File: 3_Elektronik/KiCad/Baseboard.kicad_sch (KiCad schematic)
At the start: 72 parts, among them J1 Conn_02x10_Odd_Even, J2 Conn_02x10_Odd_Even, J3 Conn_02x10_Odd_Even, J4 Conn_02x10_Odd_Even, J5 PinHeader 2,54mm 3p, J6 693072010801, J7 629722000214, Q1 2N7002K, Q2 2N7002K, SW2 430481025816, U1 ADXL375BCCZ, U2 TPS7B8601QDDARQ1, U3 TCAN334, U4 ESP32-S3-WROOM-1, U5 LSM6DSO32XTR, U6 DPS310, U7 MLX90395xLW, U8 CH224A

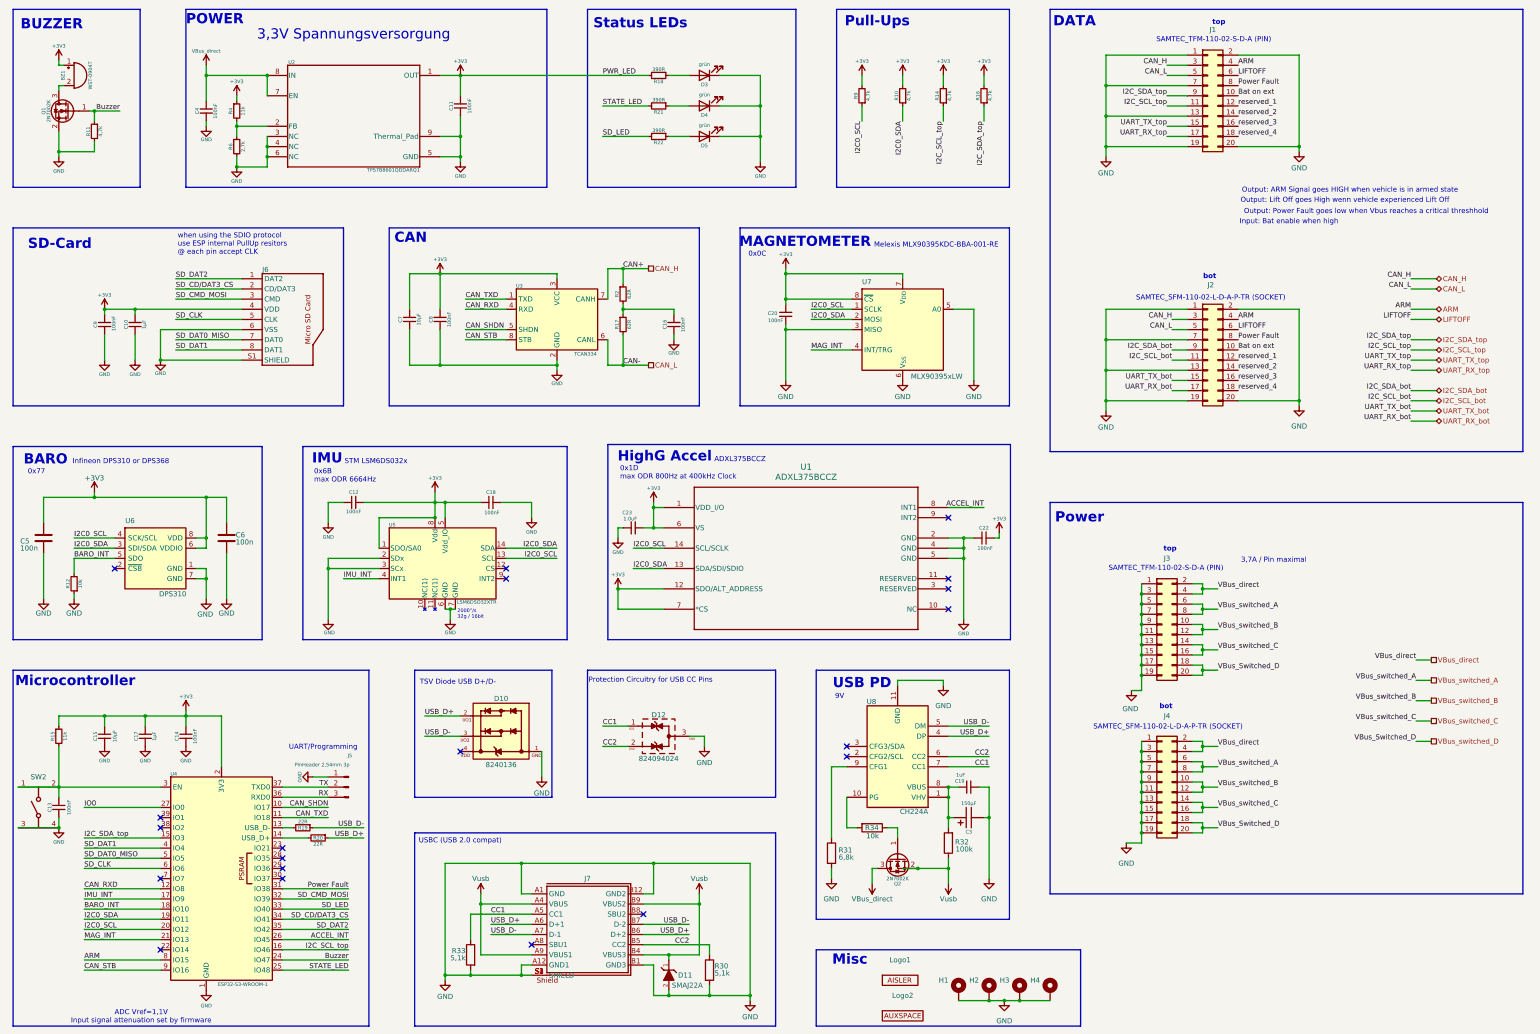
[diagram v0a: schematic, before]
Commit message: electronics: :sparkles: add BOOTSEL
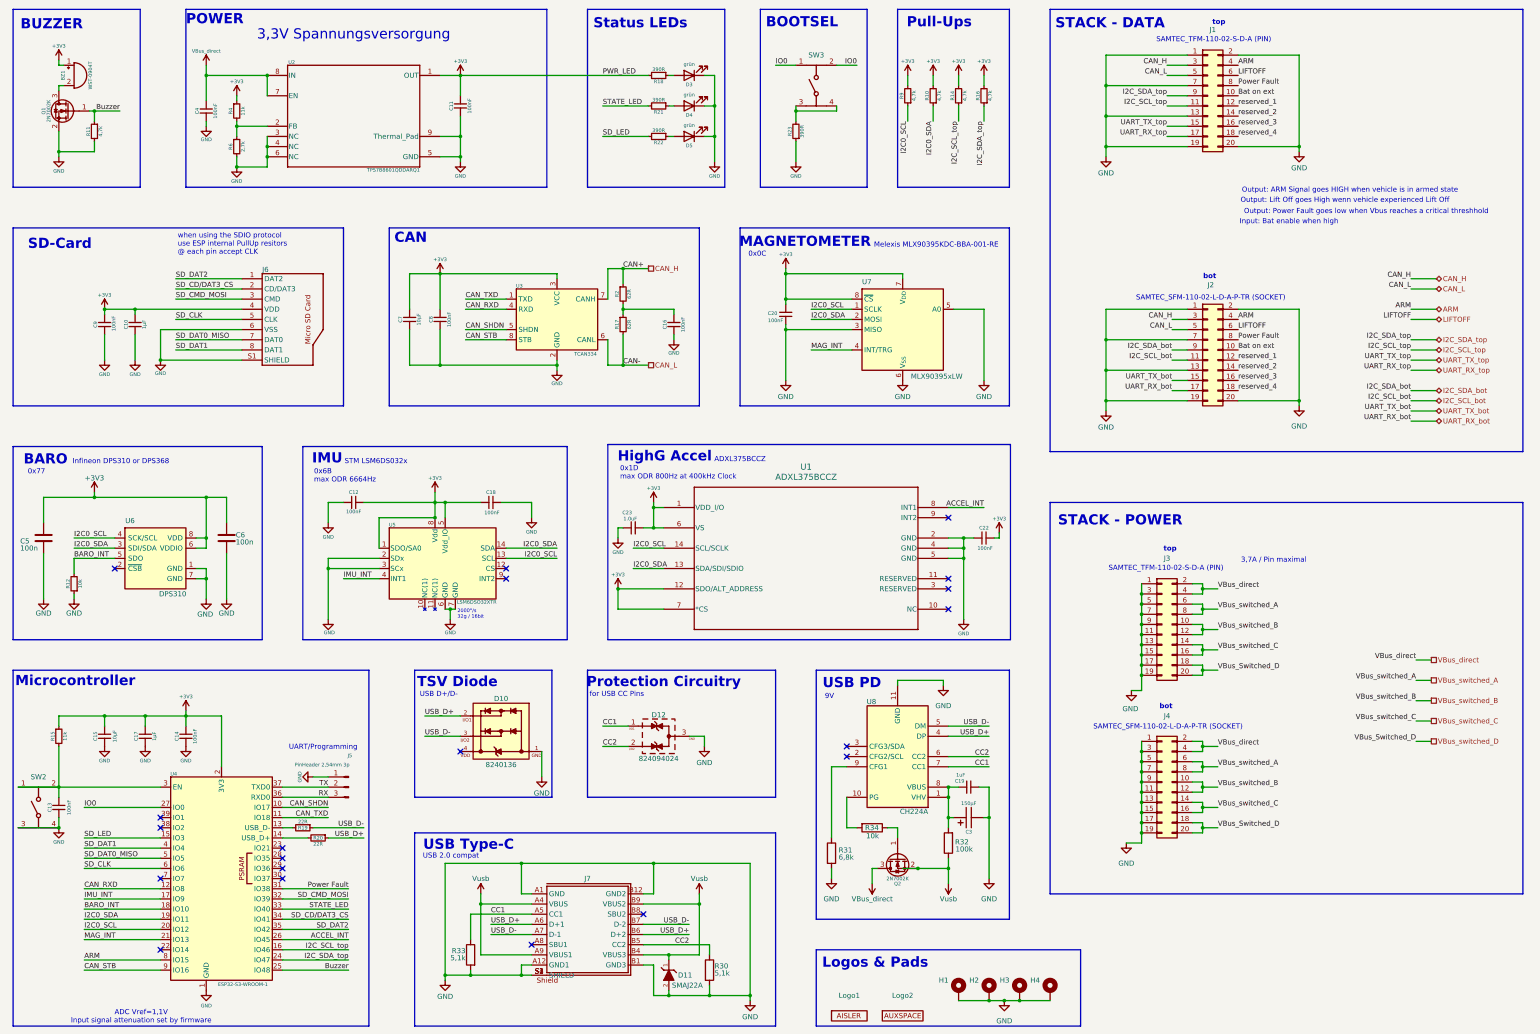
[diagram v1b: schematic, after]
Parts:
- added R23: 390R, Resistor_SMD:R_0603_1608Metric, symbol Device:R_Small
- added SW3: 430481025816, AUXSPACE:SW_Wurth_WS-TASV_430481025816, symbol AUXSPACE:430481025816
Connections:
- net Buzzer: now also U4.25 (IO48); no longer U4.24 (IO47)
- net GND: now also R23.1
- net I2C_SDA_top: now also U4.24 (IO47); no longer U4.15 (IO3)
- net IO0: now also SW3.1, SW3.2
- net SD_LED: now also U4.15 (IO3); no longer U4.33 (IO40)
- net STATE_LED: now also U4.33 (IO40); no longer U4.25 (IO48)
- new net: R23.2, SW3.3, SW3.4
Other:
- note added: "BOOTSEL"
- note added: "Logos & Pads"
- note added: "Protection Circuitry"
- note added: "STACK - DATA"
- note added: "STACK - POWER"
- note added: "TSV Diode"
- note added: "USB 2.0 compat"
- note added: "USB D+/D-"
- note added: "USB Type-C"
- note added: "for USB CC Pins"
- note removed: "DATA"
- note removed: "Misc"
- note removed: "Power"
- note removed: "Protection Circuitry for USB CC Pins"
- note removed: "TSV Diode USB D+/D-"
- note removed: "USBC (USB 2.0 compat)"
- moved on the sheet: D3, D4, D5, Logo1, R10, R14, R9

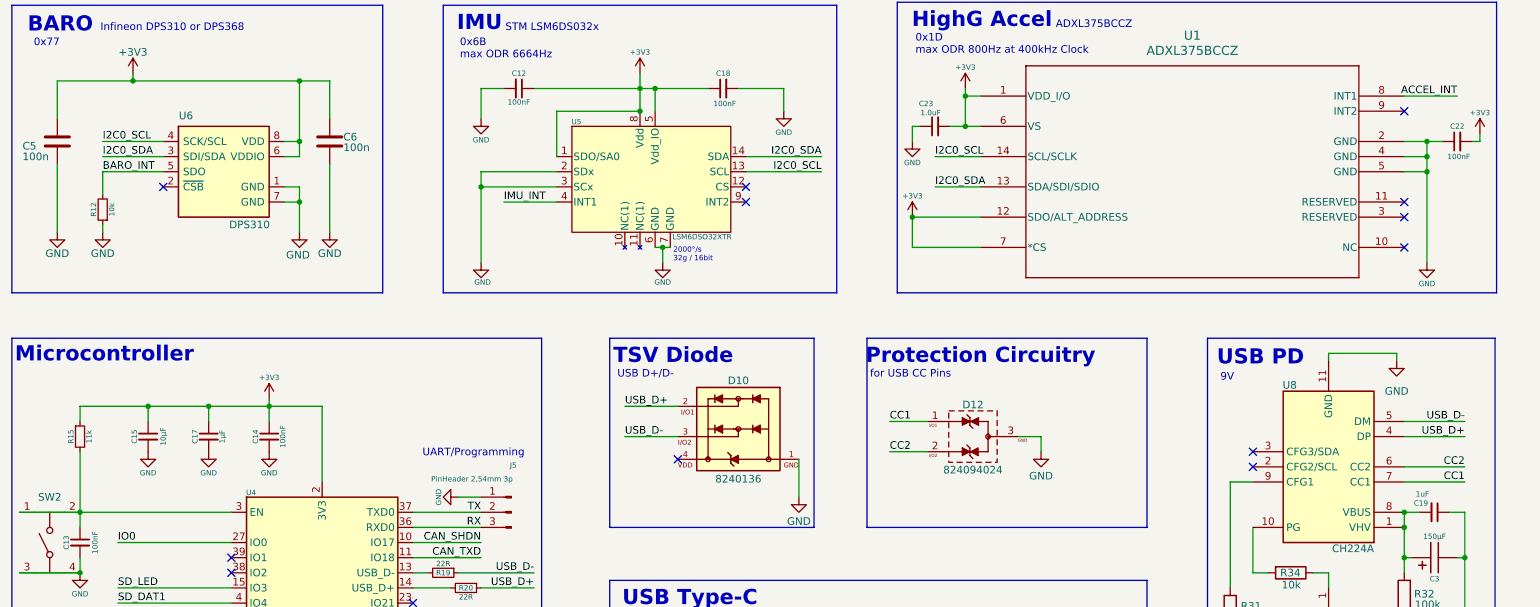
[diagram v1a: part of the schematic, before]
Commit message: BOM:              added missing datasheets, added missing partnumbers, corrected partnumbers circit diagram:   adjusted values unified writing
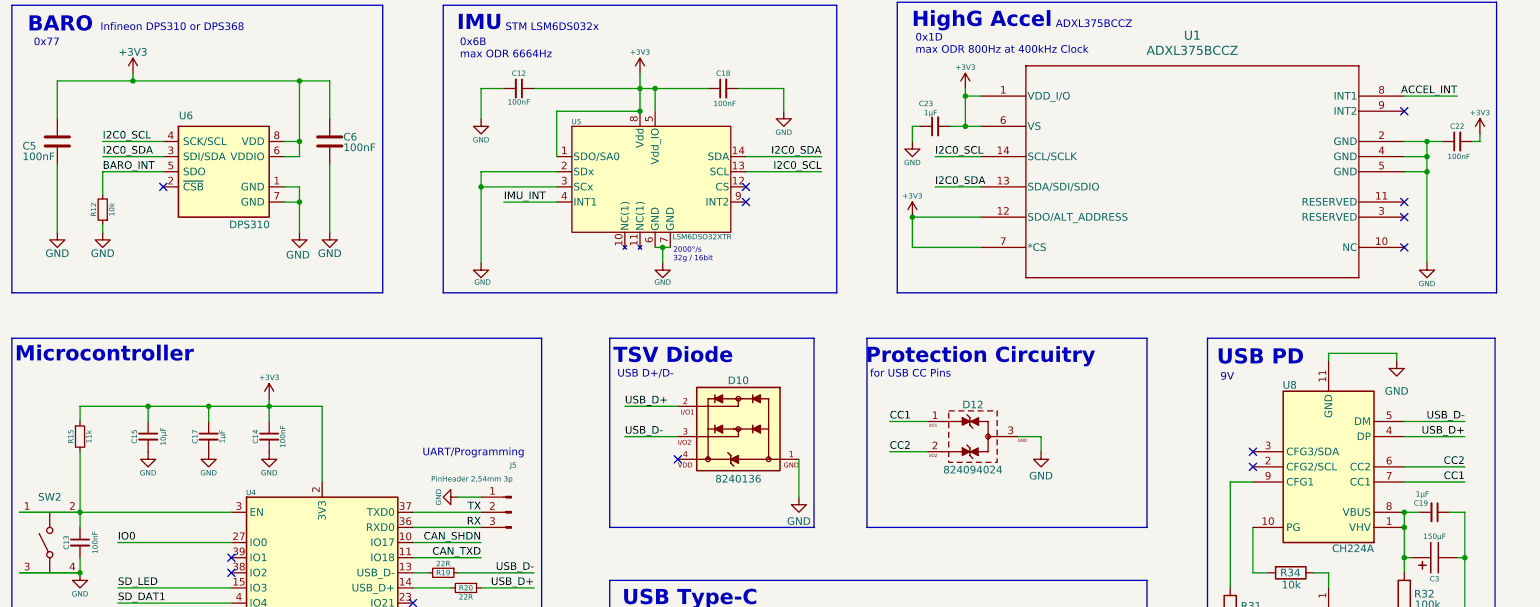
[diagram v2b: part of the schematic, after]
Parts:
- C10, C17: WE_PTNBR (none) -> 885012206076
- C11, C12, C13, C14, C16, C18, C20, C22, C4, C8, C9: WE_PTNBR (none) -> 885012206071
- C15, C7: WE_PTNBR (none) -> 885012106031
- C19: value 1uF -> 1µF; WE_PTNBR (none) -> 885012206076
- C23: value 1.0uF -> 1µF; WE_PTNBR (none) -> 885012206076
- C3: WE_PTNBR (none) -> 865060243005
- C5, C6: value 100n -> 100nF; WE_PTNBR (none) -> 885012206071
- D10: WE_PTNBR (none) -> 8240136
- D11: WE_PTNBR (none) -> 824500221
- D12: WE_PTNBR (none) -> 824094024
- D3, D4, D5: WE_PTNBR (none) -> 150060GS75020
- J1, J2, J3, J4, Logo1, Logo2: LCSC_PTNBR (none) -> not required; MOUSER_PTNBR (none) -> not required; VOELKNER_PTNBR (none) -> not required; WE_PTNBR (none) -> not required
- J5: WE_PTNBR (none) -> 61300311121
- J6: VOELKNER_PTNBR (none) -> https://www.voelkner.de/products/4073726/TRU-COMPONENTS-TC-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
- J7: WE_PTNBR (none) -> 629722000214
- Q1, Q2: LCSC_PTNBR (none) -> C3008053
- R10, R11, R14, R16, R9: WE_PTNBR (none) -> 560112116006
- R12, R34: WE_PTNBR (none) -> 560112116005
- R15, R4: WE_PTNBR (none) -> 560112116147
- R17, R2, R30, R33: LCSC_PTNBR (none) -> TODO; MOUSER_PTNBR (none) -> TODO; VOELKNER_PTNBR (none) -> TODO; WE_PTNBR (none) -> TODO
- R18, R21, R22, R23: WE_PTNBR (none) -> 560112116056
- R19, R20: WE_PTNBR (none) -> 560112116043
- R31: WE_PTNBR (none) -> 560112116007
- R32: WE_PTNBR (none) -> 560112116004
- R6: WE_PTNBR (none) -> 560112116010
- SW2, SW3: WE_PTNBR (none) -> 430481025816
- U1: LCSC_PTNBR (none) -> C481898
- U2: LCSC_PTNBR (none) -> C5189739
- U3: LCSC_PTNBR (none) -> C2871143
- U4: LCSC_PTNBR (none) -> C2913201
- U5: LCSC_PTNBR (none) -> C3663738
- U6: LCSC_PTNBR (none) -> C130156
- U7: MOUSER_PTNBR (none) -> 482-90395KLWBBA001SP
- U8: LCSC_PTNBR (none) -> C42459160

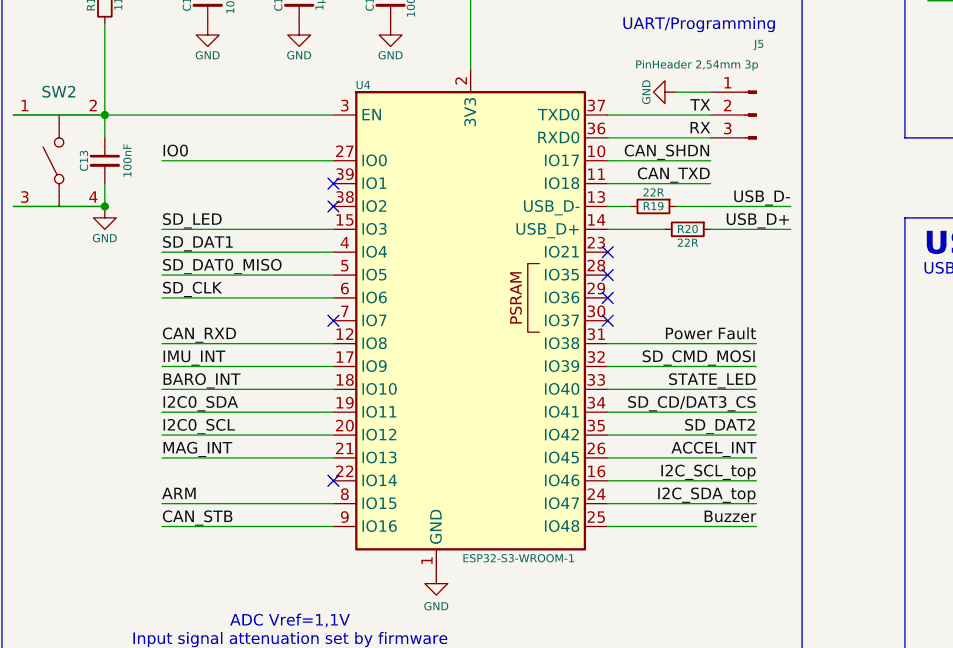
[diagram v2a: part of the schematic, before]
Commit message: added UART top/bottom and Liftoff cnonection to µC
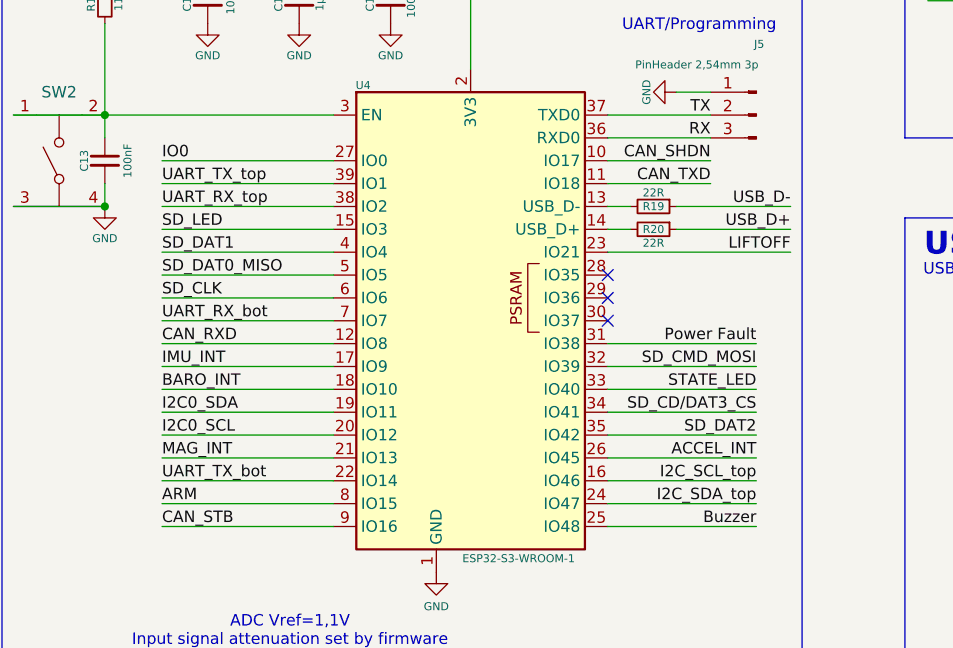
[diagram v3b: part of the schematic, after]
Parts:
- U7: LCSC_PTNBR (none) -> C1016174
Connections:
- net LIFTOFF: now also U4.23 (IO21)
- net UART_RX_bot: now also U4.7 (IO7)
- net UART_RX_top: now also U4.38 (IO2)
- net UART_TX_bot: now also U4.22 (IO14)
- net UART_TX_top: now also U4.39 (IO1)
- no-connect marks 20 -> 15
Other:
- moved on the sheet: R20
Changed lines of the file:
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@@
 	)
 	(no_connect
-		(at 88.9 231.14)
-	)
-	(no_connect
-		(at 58.42 238.76)
-	)
-	(no_connect
 		(at 229.87 208.28)
 	)
 	(no_connect
-		(at 58.42 226.06)
-	)
-	(no_connect
 		(at 144.78 163.83)
 	)
@@
 	)
 	(no_connect
-		(at 58.42 223.52)
-	)
-	(no_connect
 		(at 255.27 166.37)
 	)
-	(no_connect
-		(at 58.42 256.54)
-	)
 	(wire
 		(pts
@@
 	(wire
 		(pts
+			(xy 39.37 256.54) (xy 58.42 256.54)
+		)
+		(stroke
+			(width 0)
+			(type default)
+		)
+	)
+	(wire
+		(pts
 			(xy 148.59 234.95) (xy 129.54 234.95)
 		)
@@
 	(wire
 		(pts
-			(xy 88.9 228.6) (xy 95.25 228.6)
+			(xy 88.9 228.6) (xy 91.44 228.6)
 		)
 		(stroke
@@
 	(wire
 		(pts
+			(xy 39.37 226.06) (xy 58.42 226.06)
+		)
+		(stroke
+			(width 0)
+			(type default)
+		)
+	)
+	(wire
+		(pts
 			(xy 22.86 215.9) (xy 33.02 215.9)
 		)
@@
 	(wire
 		(pts
+			(xy 39.37 223.52) (xy 58.42 223.52)
+		)
+		(stroke
+			(width 0)
+			(type default)
+		)
+	)
+	(wire
+		(pts
 			(xy 190.5 252.73) (xy 179.07 252.73)
 		)
@@
 	(wire
 		(pts
-			(xy 100.33 228.6) (xy 109.22 228.6)
+			(xy 96.52 228.6) (xy 109.22 228.6)
 		)
 		(stroke
@@
 	(wire
 		(pts
+			(xy 109.22 231.14) (xy 88.9 231.14)
+		)
+		(stroke
+			(width 0)
+			(type default)
+		)
+	)
+	(wire
+		(pts
 			(xy 148.59 242.57) (xy 151.13 242.57)
 		)
@@
 	(wire
 		(pts
+			(xy 39.37 238.76) (xy 58.42 238.76)
+		)
+		(stroke
+			(width 0)
+			(type default)
+		)
+	)
+	(wire
+		(pts
 			(xy 214.63 86.36) (xy 214.63 87.63)
 		)
@@
 		)
 	)
+	(label "LIFTOFF"
+		(at 109.22 231.14 180)
+		(effects
+			(font
+				(size 1.27 1.27)
+			)
+			(justify right bottom)
+		)
+	)
+	(label "UART_RX_bot"
+		(at 39.37 238.76 0)
+		(effects
+			(font
+				(size 1.27 1.27)
+			)
+			(justify left bottom)
+		)
+	)
 	(label "UART_TX_bot"
 		(at 370.84 121.92 180)
@@
 		)
 	)
+	(label "UART_TX_bot"
+		(at 39.37 256.54 0)
+		(effects
+			(font
+				(size 1.27 1.27)
+			)
+			(justify left bottom)
+		)
+	)
 	(label "LIFTOFF"
 		(at 370.84 99.06 180)
@@
 		)
 	)
+	(label "UART_RX_top"
+		(at 39.37 226.06 0)
+		(effects
+			(font
+				(size 1.27 1.27)
+			)
+			(justify left bottom)
+		)
+	)
 	(label "LIFTOFF"
 		(at 327.66 38.1 0)
@@
 		)
 	)
+	(label "UART_TX_top"
+		(at 39.37 223.52 0)
+		(effects
+			(font
+				(size 1.27 1.27)
+			)
+			(justify left bottom)
+		)
+	)
 	(label "CAN_H"
 		(at 370.84 88.9 180)
@@
 	(symbol
 		(lib_id "Device:R_Small")
-		(at 97.79 228.6 270)
+		(at 93.98 228.6 270)
 		(unit 1)
 		(body_style 1)
@@
 		(dnp no)
 		(property "Reference" "R20"
-			(at 97.79 228.6 90)
+			(at 93.98 228.6 90)
 			(show_name no)
 			(do_not_autoplace no)
@@
 		)
 		(property "Value" "22R"
-			(at 97.79 230.124 90)
+			(at 93.98 230.124 90)
 			(show_name no)
 			(do_not_autoplace no)
@@
 		)
 		(property "Footprint" "Resistor_SMD:R_0603_1608Metric"
-			(at 97.79 228.6 0)
+			(at 93.98 228.6 0)
 			(hide yes)
 			(show_name no)
@@
 		)
 		(property "Datasheet" "https://www.we-online.com/components/products/datasheet/560112116043.pdf"
-			(at 97.79 228.6 0)
+			(at 93.98 228.6 0)
 			(hide yes)
 			(show_name no)
@@
 		)
 		(property "Description" "Resistor, small symbol"
-			(at 97.79 228.6 0)
+			(at 93.98 228.6 0)
 			(hide yes)
 			(show_name no)
@@
 		)
 		(property "LCSC_PTNBR" ""
-			(at 97.79 228.6 90)
+			(at 93.98 228.6 90)
 			(hide yes)
 			(show_name no)
@@
 		)
 		(property "WE_PTNBR" "560112116043"
-			(at 97.79 228.6 90)
+			(at 93.98 228.6 90)
 			(hide yes)
 			(show_name no)
@@
 		)
 		(property "VOELKNER_PTNBR" ""
-			(at 97.79 228.6 90)
+			(at 93.98 228.6 90)
 			(hide yes)
 			(show_name no)
@@
 		)
 		(property "MOUSER_PTNBR" ""
-			(at 97.79 228.6 90)
+			(at 93.98 228.6 90)
 			(hide yes)
 			(show_name no)
@@
 			)
 		)
-		(property "LCSC_PTNBR" ""
+		(property "LCSC_PTNBR" "C1016174"
 			(at 243.84 101.6 0)
 			(hide yes)

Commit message: fix: :bug: drc errors
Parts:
- added C21: 4.7µF, Capacitor_SMD:C_0603_1608Metric, symbol Device:C_Small
- added C24: 100nF, Capacitor_SMD:C_0603_1608Metric, symbol Device:C_Small
- C23: value 1µF -> 100nF; WE_PTNBR 885012206076 -> 885012206071
- U1: value ADXL375BCCZ -> LSM6DSV320XTR; footprint AUXSPACE:LGA_CC-14-1_ADI -> LGA-14L_2p5X3X0p83_STM; symbol AUXSPACE:ADXL375BCCZ -> 2026-10-07_23-10-11:LSM6DSV320XTR; LCSC_PTNBR C481898 -> (none)
- U7: value MLX90395xLW -> IST8310; footprint Package_SO:SOIC-8_3.9x4.9mm_P1.27mm -> Package_LGA:LGA-16_3x3mm_P0.5mm; symbol Sensor_Magnetic:MLX90395xLW -> Sensor_Magnetic:IST8310; LCSC_PTNBR C1016174 -> (none); MOUSER_PTNBR 482-90395KLWBBA001SP -> (none)
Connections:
- net +3V3: now also C20.1, U1.2 (SDX), U1.3 (SCX), U1.5 (VDDIO), U1.8 (VDD), U7.13 (DVDD), U7.2 (AVDD), C24.2; no longer C20.2, U1.6 (VS), U1.7 (*CS), U5.1 (SDO/SA0), U7.7 (V_{DD}), U7.8 (~{CS})
- net BARO_INT: now also U4.25 (IO48); no longer U4.18 (IO10)
- net Buzzer: now also U4.26 (IO45); no longer U4.25 (IO48)
- net GND: now also C20.2, U1.6 (GND), U1.7 (GND), U5.1 (SDO/SA0), U7.11 (VSS), U7.9 (VSS), C21.2, C24.1; no longer C20.1, U1.2 (GND), U1.4 (GND), U1.5 (GND), U7.3 (MISO), U7.5 (A0), U7.6 (V_{SS})
- net I2C0_SCL: now also U1.13 (SCL); no longer U1.14 (SCL/SCLK)
- net I2C0_SDA: now also U1.14 (SDA), U7.16 (SDA); no longer U1.13 (SDA/SDI/SDIO), U7.2 (MOSI)
- net I2C_SCL_top: now also U4.22 (IO14); no longer U4.16 (IO46)
- net I2C_SDA_top: now also U4.21 (IO13); no longer U4.24 (IO47)
- net IMU_INT: now also U4.24 (IO47); no longer U4.17 (IO9)
- net LIFTOFF: now also U4.16 (IO46); no longer U4.23 (IO21)
- net UART_TX_bot: now also U4.17 (IO9); no longer U4.22 (IO14)
- net ACCEL_INT2: now reaches U1.9 (INT2)
- removed net ACCEL_INT: U1.8 (INT1), U4.26 (IO45)
- net MAG_INT: no longer names the net of U7.4 (NC)
- net MAG_INT: no longer U4.21 (IO13)
- new net: C21.1, U7.10 (C1)
- new net ACCEL_INT1: U1.4 (INT1), U4.18 (IO10)
- no-connect marks 15 -> 19
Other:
- note added: "0x0E"
- note added: "0x6A max ODR 6664Hz"
- note added: "0x6B max ODR 480 Hz"
- note added: "LSM6DSV320XTR"
- note added: "isentek IST8310"
- note removed: "0x0C"
- note removed: "0x1D max ODR 800Hz at 400kHz Clock"
- note removed: "0x6B max ODR 6664Hz"
- note removed: "ADXL375BCCZ"
- note removed: "Melexis MLX90395KDC-BBA-001-RE"
- moved on the sheet: C20, C22, U1
